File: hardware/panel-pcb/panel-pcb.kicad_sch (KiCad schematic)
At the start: 128 parts, among them J1 USB_C_Receptacle_USB2.0_16P, J10 RS-485 OUT, J11 12V_OUT, J2 SWD, J3 FSR North, J4 FSR East, J5 12V_IN, J6 FSR South, J7 FSR West, J8 RS-485 IN, J9 INT OUT, SW1 PANEL_ID, SW2 BOOTSEL, SW3 RS-485 Termination, U1 RP2040, U2 THVD1419, U3 W25Q32JV, U4 SN74AHCT125, U5 AMS1117-5.0, U6 AMS1117-3.3, X1 12MHz

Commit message: Pin down final three connector parts: USB-C = GCT USB4085-GF-A (all-TH; LCSC 'vertical DIP' parts are actually SMD), termination switch = E-Switch EG2201A, INT = KF301-style 1P 5.08mm; assign J1/J9 footprints
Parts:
- J1: footprint (none) -> Connector_USB:USB_C_Receptacle_GCT_USB4085
- J9: footprint (none) -> TerminalBlock:TerminalBlock_bornier-1_P5.08mm
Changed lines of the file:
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@@
 			)
 		)
-		(property "Footprint" ""
+		(property "Footprint" "Connector_USB:USB_C_Receptacle_GCT_USB4085"
 			(at 153.67 158.75 0)
 			(hide yes)
@@
 			)
 		)
-		(property "Footprint" ""
+		(property "Footprint" "TerminalBlock:TerminalBlock_bornier-1_P5.08mm"
 			(at 248.92 270.51 0)
 			(hide yes)

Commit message: Import EG2201A footprint (SnapEDA) into project lib, assign to SW3; fix SW1/SW3 mixup in docs
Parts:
- SW3: footprint (none) -> panel-pcb:SW_EG2201A
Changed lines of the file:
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@@
 			)
 		)
-		(property "Footprint" ""
+		(property "Footprint" "panel-pcb:SW_EG2201A"
 			(at 38.1 95.25 0)
 			(hide yes)

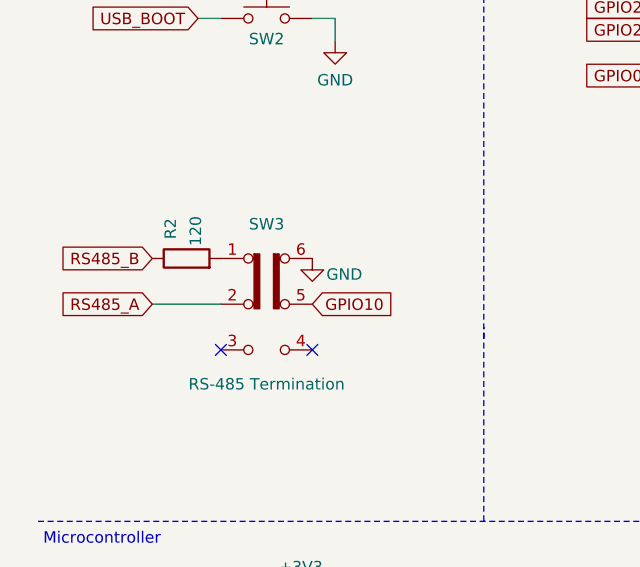
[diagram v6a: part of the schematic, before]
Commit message: SW3: swap generic DPDT symbol for SnapEDA EG2201A + fix termination-sense polarity
- EG2201A symbol embedded + added to new project symbol lib (panel-pcb.kicad_sym
  + sym-lib-table); reads as one physical slide, matches footprint pin layout
- Rewired for new pin geometry: RS485_A -> pin 2 (common), R2 120R relocated to
  pin 1, GPIO10 label -> pin 5, GND moved pin 6 -> pin 4 so the position that
  inserts the 120R also reads LOW = terminated (was inverted), pins 3/6 NC
- Netlist-verified pin-exact; ERC 0 errors
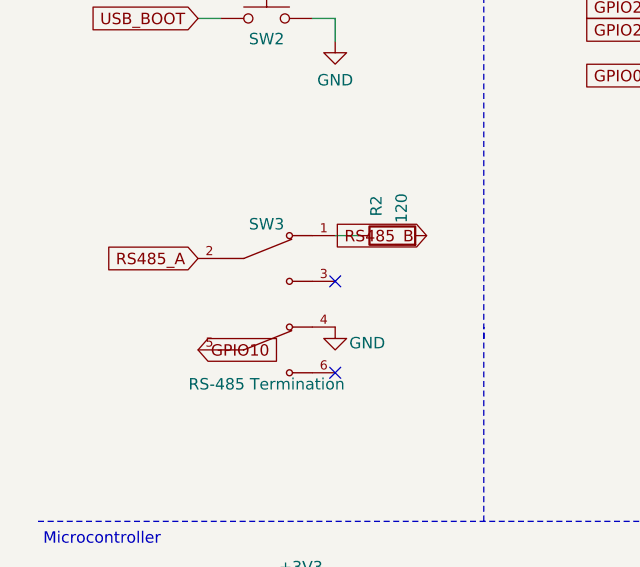
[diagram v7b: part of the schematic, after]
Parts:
- SW3: symbol Switch:SW_Slide_DPDT -> panel-pcb:EG2201A
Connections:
- net GND: now also SW3.4; no longer SW3.6 (C)
- net RS485_B: now also R2.2; no longer R2.1
- net at SW3.1: now also R2.1; no longer R2.2
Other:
- moved on the sheet: R2
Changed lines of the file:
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@@
 	)
 	(no_connect
-		(at 33.02 100.33)
-	)
-	(no_connect
 		(at 391.16 151.13)
 	)
@@
 	)
 	(no_connect
-		(at 43.18 100.33)
-	)
-	(no_connect
 		(at 226.06 74.93)
 	)
@@
 	(wire
 		(pts
-			(xy 25.4 95.25) (xy 33.02 95.25)
-		)
-		(stroke
-			(width 0)
-			(type default)
-		)
-	)
-	(wire
-		(pts
 			(xy 260.35 53.34) (xy 233.68 53.34)
 		)
@@
 	(global_label "RS485_B"
 		(shape input)
-		(at 25.4 90.17 180)
+		(at 55.88 87.63 0)
 		(fields_autoplaced yes)
 		(effects
@@
 	(global_label "RS485_A"
 		(shape input)
-		(at 25.4 95.25 180)
+		(at 30.48 90.17 180)
 		(fields_autoplaced yes)
 		(effects
@@
 	(global_label "GPIO10"
 		(shape input)
-		(at 43.18 95.25 0)
+		(at 30.48 100.33 180)
 		(fields_autoplaced yes)
 		(effects
@@
 	)
 	(symbol
-		(lib_id "Switch:SW_Slide_DPDT")
+		(lib_id "panel-pcb:EG2201A")
 		(at 38.1 95.25 0)
 		(unit 1)
@@
 			)
 		)
-		(property "Description" "DPDT slide switch, RS-485 termination. Common pins (2, 5) are the switch wiper; pole 1 (pins 1-3) routes the 120R termination resistor in/out of the A/B pair, pole 2 (pins 4-6) ganged on the same physical actuator reports termination state to GPIO10. See docs/MODULAR_PANEL_COUNT.md."
+		(property "Description" "DPDT slide switch, RS-485 termination. Common pins (2, 5) are the switch wiper; pole 1 (pins 1-3) routes the 120R termination resistor in/out of the A/B pair, pole 2 (pins 4-6) ganged on the same physical actuator reports termination state to GPIO10 (pin 4 = GND so the position that inserts the 120R also reads LOW = terminated). See docs/MODULAR_PANEL_COUNT.md."
 			(at 38.1 95.25 0)
 			(hide yes)
@@
 	(symbol
 		(lib_id "power:GND")
-		(at 43.18 90.17 0)
+		(at 45.72 97.79 0)
 		(unit 1)
 		(body_style 1)
@@
 		(dnp no)
 		(property "Reference" "#PWR010"
-			(at 43.18 95.25 0)
+			(at 45.72 102.87 0)
 			(hide yes)
 			(show_name no)
@@
 		)
 		(property "Value" "GND"
-			(at 46.736 91.948 0)
+			(at 49.28 99.57 0)
 			(show_name no)
 			(do_not_autoplace no)
@@
 		)
 		(property "Footprint" ""
-			(at 43.18 90.17 0)
+			(at 45.72 97.79 0)
 			(hide yes)
 			(show_name no)
@@
 		)
 		(property "Datasheet" ""
-			(at 43.18 90.17 0)
+			(at 45.72 97.79 0)
 			(hide yes)
 			(show_name no)
@@
 		)
 		(property "Description" ""
-			(at 43.18 90.17 0)
+			(at 45.72 97.79 0)
 			(hide yes)
 			(show_name no)
@@
 	(symbol
 		(lib_id "Device:R")
-		(at 29.21 90.17 90)
+		(at 52.07 87.63 90)
 		(unit 1)
 		(body_style 1)
@@
 		(dnp no)
 		(property "Reference" "R2"
-			(at 27.432 86.868 0)
+			(at 50.29 84.33 0)
 			(show_name no)
 			(do_not_autoplace no)
@@
 		)
 		(property "Value" "120"
-			(at 30.226 87.122 0)
+			(at 53.09 84.58 0)
 			(show_name no)
 			(do_not_autoplace no)
@@
 		)
 		(property "Footprint" "Resistor_SMD:R_0603_1608Metric"
-			(at 29.21 90.17 0)
+			(at 52.07 87.63 0)
 			(hide yes)
 			(show_name no)
@@
 		)
 		(property "Datasheet" ""
-			(at 29.21 90.17 0)
+			(at 52.07 87.63 0)
 			(hide yes)
 			(show_name no)
@@
 		)
 		(property "Description" "RS-485 bus termination resistor. In-circuit only when SW2 pole 1 is in the terminated position."
-			(at 29.21 90.17 0)
+			(at 52.07 87.63 0)
 			(hide yes)
 			(show_name no)
@@
 		)
 	)
+	(wire
+		(pts
+			(xy 45.72 87.63) (xy 48.26 87.63)
+		)
+		(stroke
+			(width 0)
+			(type default)
+		)
+	)
+	(no_connect
+		(at 45.72 92.71)
+	)
+	(no_connect
+		(at 45.72 102.87)
+	)
 	(sheet_instances

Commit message: Pre-layout audit fixes: R2 -> 120R (RKM consistency), remove 2 drag-debris wire stubs, replace defunct bornier footprint with hand-drawn KF301-1P (verify dims at order)
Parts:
- J9: footprint TerminalBlock:TerminalBlock_bornier-1_P5.08mm -> panel-pcb:TerminalBlock_KF301-1P_P5.08mm
- R2: value 120 -> 120R
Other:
- note added: "+12.0V"
- note added: "+3V3"
- note added: "+5.0V"
- moved on the sheet: C10, C11, C13, C15, C20, C37, C38, C44, C50, D12, D23, R2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
